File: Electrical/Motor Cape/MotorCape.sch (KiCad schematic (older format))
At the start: 15 parts, among them J1 back_right motor, J11 flag_wheel servo, J2 front_right motor, J3 back_left motor, J4 front_left motor, J5 draw_bridge motor, J6 flag_wheel motor, J7 i2c bus connector, J9 Raspberry_Pi_2_3, U1 MotorControl Left, U2 MotorControl Right, U3 MotorControl Top

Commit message: worked more on motor cape
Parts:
- removed U1: MotorControl Left, symbol MotorControl
- removed U2: MotorControl Right, symbol MotorControl
- removed U3: MotorControl Top, symbol MotorControl
- added P1: Shifter_Front_HI, Pin_Headers:Pin_Header_Straight_1x06, symbol CONN_01X06
- added P10: Controller 2_2, Terminal_Blocks:TerminalBlock_Pheonix_MPT-2.54mm_6pol, symbol CONN_01X06
- added P11: Controller 3_1, Pin_Headers:Pin_Header_Straight_1x05, symbol CONN_01X05
- added P12: Controller 3_2, Terminal_Blocks:TerminalBlock_Pheonix_MPT-2.54mm_6pol, symbol CONN_01X06
- added P2: Shifter_Front_LO, Pin_Headers:Pin_Header_Straight_1x06, symbol CONN_01X06
- added P3: Shifter_Back_HI, Pin_Headers:Pin_Header_Straight_1x06, symbol CONN_01X06
- added P4: Shifter_Back_LO, Pin_Headers:Pin_Header_Straight_1x06, symbol CONN_01X06
- added P5: Shifter_Misc_HI, Pin_Headers:Pin_Header_Straight_1x06, symbol CONN_01X06
- added P6: Shifter_Misc_LO, Pin_Headers:Pin_Header_Straight_1x06, symbol CONN_01X06
- added P7: Controller 1_1, Pin_Headers:Pin_Header_Straight_1x05, symbol CONN_01X05
- added P8: Controller 1_2, Terminal_Blocks:TerminalBlock_Pheonix_MPT-2.54mm_6pol, symbol CONN_01X06
- added P9: Controller 2_1, Pin_Headers:Pin_Header_Straight_1x05, symbol CONN_01X05
- ARD1: footprint (none) -> MotorCapeComponents:Arduino_Due_Shield
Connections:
- net labels removed: BL_A-H, BL_A-L, BL_B-H, BL_B-L, BR_A-H, BR_A-L, BR_B-H, BR_B-L, DB_A-H, DB_A-L, DB_B-H, DB_B-L, FL_A-L, FL_B-L, FR_A-H, FR_A-L, FR_B-H, FR_B-L, FW_A-H, FW_A-L, FW_B-H, FW_B-L
- wire segments 110 -> 247
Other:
- moved on the sheet: J2

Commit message: added gud stuff
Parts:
- removed Battery1: pcie_8pin power connector, symbol Conn_02x04_Top_Bottom
- added P13: battery stuff, Pin_Headers:Pin_Header_Straight_1x02, symbol CONN_01X02
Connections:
- net +5V: no longer P2.4 (P4), P4.4 (P4), P6.4 (P4)
- net Earth: now also P13.2 (P2)
- net +12V: now reaches F1.2
- net +12V: now also P13.1 (P1)
- new net +3V3: P2.4 (P4), P4.4 (P4), P6.4 (P4)
- no-connect marks 88 -> 89
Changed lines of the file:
@@
-$EndComp
-$Comp
-L Conn_02x04_Top_Bottom Battery1
-U 1 1 5A6B59ED
-P 1500 2950
-F 0 "Battery1" H 1550 3150 50  0000 C CNN
-F 1 "pcie_8pin power connector" H 1550 2650 50  0000 C CNN
-F 2 "" H 1500 2950 50  0001 C CNN
-F 3 "" H 1500 2950 50  0001 C CNN
-	1    1500 2950
-	-1   0    0    1
 $EndComp
 $Comp
@@
 F1 "level_shifters.sch" 60
 $EndSheet
-Text GLabel 3150 3500 2    60   Input ~ 0
-FL_B-H
-Text GLabel 3150 3600 2    60   Input ~ 0
-FL_A-H
 $Comp
 L Raspberry_Pi_2_3 J9
@@
 Text GLabel 2200 2900 2    60   Input ~ 0
 MOTOR_PWR
-Text GLabel 2200 3100 2    60   Input ~ 0
+Text GLabel 1250 2700 0    60   Input ~ 0
 MOTOR_GND
-$Comp
-L Arduino_Due_Shield ARD1
-U 1 1 5A86C034
-P 5850 2400
-F 0 "ARD1" V 5950 2400 60  0000 C CNN
-F 1 "Arduino_Due_Shield" V 5750 2400 60  0000 C CNN
-F 2 "MotorCapeComponents:Arduino_Due_Shield" H 6550 5150 60  0001 C CNN
-F 3 "" H 6550 5150 60  0001 C CNN
-	1    5850 2400
-	0    1    1    0
-$EndComp
 $Comp
 L CONN_01X06 P1
@@
 $EndComp
 $Comp
-L +5V #PWR026
-U 1 1 5A8FD9AD
-P 9300 4350
-F 0 "#PWR026" H 9300 4200 50  0001 C CNN
-F 1 "+5V" H 9300 4490 50  0000 C CNN
-F 2 "" H 9300 4350 50  0001 C CNN
-F 3 "" H 9300 4350 50  0001 C CNN
-	1    9300 4350
-	1    0    0    -1
-$EndComp
-$Comp
-L Earth #PWR027
+L Earth #PWR026
 U 1 1 5A8FD9EB
 P 9400 4350
-F 0 "#PWR027" H 9400 4100 50  0001 C CNN
+F 0 "#PWR026" H 9400 4100 50  0001 C CNN
 F 1 "Earth" H 9400 4200 50  0001 C CNN
 F 2 "" H 9400 4350 50  0001 C CNN
@@
 $EndComp
 $Comp
-L Earth #PWR028
+L Earth #PWR027
 U 1 1 5A901DF0
 P 6600 7200
-F 0 "#PWR028" H 6600 6950 50  0001 C CNN
+F 0 "#PWR027" H 6600 6950 50  0001 C CNN
 F 1 "Earth" H 6600 7050 50  0001 C CNN
 F 2 "" H 6600 7200 50  0001 C CNN
@@
 $EndComp
 $Comp
-L Earth #PWR029
+L Earth #PWR028
 U 1 1 5A901E80
 P 6600 6800
-F 0 "#PWR029" H 6600 6550 50  0001 C CNN
+F 0 "#PWR028" H 6600 6550 50  0001 C CNN
 F 1 "Earth" H 6600 6650 50  0001 C CNN
 F 2 "" H 6600 6800 50  0001 C CNN
@@
 $EndComp
 $Comp
-L +5V #PWR030
-U 1 1 5A901F49
-P 6500 7200
-F 0 "#PWR030" H 6500 7050 50  0001 C CNN
-F 1 "+5V" H 6500 7340 50  0000 C CNN
-F 2 "" H 6500 7200 50  0001 C CNN
-F 3 "" H 6500 7200 50  0001 C CNN
-	1    6500 7200
-	1    0    0    -1
-$EndComp
-$Comp
-L +5V #PWR031
+L +5V #PWR029
 U 1 1 5A902038
 P 6500 6800
-F 0 "#PWR031" H 6500 6650 50  0001 C CNN
+F 0 "#PWR029" H 6500 6650 50  0001 C CNN
 F 1 "+5V" H 6500 6940 50  0000 C CNN
 F 2 "" H 6500 6800 50  0001 C CNN
@@
 $EndComp
 $Comp
-L +5V #PWR032
+L +5V #PWR030
 U 1 1 5A906051
 P 1100 5250
-F 0 "#PWR032" H 1100 5100 50  0001 C CNN
+F 0 "#PWR030" H 1100 5100 50  0001 C CNN
 F 1 "+5V" H 1100 5390 50  0000 C CNN
 F 2 "" H 1100 5250 50  0001 C CNN
@@
 $EndComp
 $Comp
-L +5V #PWR033
-U 1 1 5A90614E
-P 1100 5950
-F 0 "#PWR033" H 1100 5800 50  0001 C CNN
-F 1 "+5V" H 1100 6090 50  0000 C CNN
-F 2 "" H 1100 5950 50  0001 C CNN
-F 3 "" H 1100 5950 50  0001 C CNN
-	1    1100 5950
-	-1   0    0    -1
-$EndComp
-$Comp
-L Earth #PWR034
+L Earth #PWR031
 U 1 1 5A9062E9
 P 1200 5250
-F 0 "#PWR034" H 1200 5000 50  0001 C CNN
+F 0 "#PWR031" H 1200 5000 50  0001 C CNN
 F 1 "Earth" H 1200 5100 50  0001 C CNN
 F 2 "" H 1200 5250 50  0001 C CNN
@@
 $EndComp
 $Comp
-L Earth #PWR035
+L Earth #PWR032
 U 1 1 5A906333
 P 1200 5950
-F 0 "#PWR035" H 1200 5700 50  0001 C CNN
+F 0 "#PWR032" H 1200 5700 50  0001 C CNN
 F 1 "Earth" H 1200 5800 50  0001 C CNN
 F 2 "" H 1200 5950 50  0001 C CNN
@@
 Wire Wire Line
 	3650 6200 3650 6450
+$Comp
+L +3.3V #PWR033
+U 1 1 5A98D0A1
+P 10350 4400
+F 0 "#PWR033" H 10350 4250 50  0001 C CNN
+F 1 "+3.3V" H 10350 4540 50  0000 C CNN
+F 2 "" H 10350 4400 50  0000 C CNN
+F 3 "" H 10350 4400 50  0000 C CNN
+	1    10350 4400
+	-1   0    0    1
+$EndComp
+$Comp
+L +3.3V #PWR034
+U 1 1 5A98D26D
+P 6500 7200
+F 0 "#PWR034" H 6500 7050 50  0001 C CNN
+F 1 "+3.3V" H 6500 7340 50  0000 C CNN
+F 2 "" H 6500 7200 50  0000 C CNN
+F 3 "" H 6500 7200 50  0000 C CNN
+	1    6500 7200
+	1    0    0    -1
+$EndComp
+$Comp
+L +3.3V #PWR035
+U 1 1 5A98D68F
+P 1100 5950
+F 0 "#PWR035" H 1100 5800 50  0001 C CNN
+F 1 "+3.3V" H 1100 6090 50  0000 C CNN
+F 2 "" H 1100 5950 50  0000 C CNN
+F 3 "" H 1100 5950 50  0000 C CNN
+	1    1100 5950
+	1    0    0    -1
+$EndComp
+$Comp
+L CONN_01X02 P13
+U 1 1 5A98ECA7
+P 1550 2850
+F 0 "P13" H 1550 3000 50  0000 C CNN
+F 1 "battery stuff" V 1650 2850 50  0000 C CNN
+F 2 "Pin_Headers:Pin_Header_Straight_1x02" H 1550 2850 50  0001 C CNN
+F 3 "" H 1550 2850 50  0000 C CNN
+	1    1550 2850
+	-1   0    0    1
+$EndComp
+$Comp
+L +12V #PWR036
+U 1 1 5A98F2CD
+P 1750 2900
+F 0 "#PWR036" H 1750 2750 50  0001 C CNN
+F 1 "+12V" H 1750 3040 50  0000 C CNN
+F 2 "" H 1750 2900 50  0000 C CNN
+F 3 "" H 1750 2900 50  0000 C CNN
+	1    1750 2900
+	-1   0    0    1
+$EndComp
+$Comp
+L Earth #PWR037
+U 1 1 5A98F376
+P 1750 2750
+F 0 "#PWR037" H 1750 2500 50  0001 C CNN
+F 1 "Earth" H 1750 2600 50  0001 C CNN
+F 2 "" H 1750 2750 50  0001 C CNN
+F 3 "" H 1750 2750 50  0001 C CNN
+	1    1750 2750
+	1    0    0    1
+$EndComp
+Wire Wire Line
+	1900 2900 1750 2900
+Wire Wire Line
+	1750 2800 1750 2750
+NoConn ~ 5000 1200
+$Comp
+L PWR_FLAG #FLG038
+U 1 1 5A9910A8
+P 1850 3250
+F 0 "#FLG038" H 1850 3345 50  0001 C CNN
+F 1 "PWR_FLAG" H 1850 3430 50  0000 C CNN
+F 2 "" H 1850 3250 50  0000 C CNN
+F 3 "" H 1850 3250 50  0000 C CNN
+	1    1850 3250
+	-1   0    0    1
+$EndComp
+Wire Wire Line
+	1850 3250 1850 2900
+Connection ~ 1850 2900
+$Comp
+L PWR_FLAG #FLG039
+U 1 1 5A991593
+P 10050 4350
+F 0 "#FLG039" H 10050 4445 50  0001 C CNN
+F 1 "PWR_FLAG" H 10050 4530 50  0000 C CNN
+F 2 "" H 10050 4350 50  0000 C CNN
+F 3 "" H 10050 4350 50  0000 C CNN
+	1    10050 4350
+	-1   0    0    1
+$EndComp
+Wire Wire Line
+	10350 4400 10350 4350
+Wire Wire Line
+	10350 4350 10050 4350
+Wire Wire Line
+	10050 4350 10050 4200
+Wire Wire Line
+	10050 4200 9300 4200
+Wire Wire Line
+	9300 4200 9300 4350
+$Comp
+L Arduino_Due_Shield ARD1
+U 1 1 5A993409
+P 5850 2400
+F 0 "ARD1" V 5950 2400 60  0000 C CNN
+F 1 "Arduino_Due_Shield" V 5750 2400 60  0000 C CNN
+F 2 "MotorCapeComponents:Arduino_Due_Shield" H 6550 5150 60  0001 C CNN
+F 3 "" H 6550 5150 60  0001 C CNN
+	1    5850 2400
+	0    1    1    0
+$EndComp
 $EndSCHEMATC

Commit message: pushing aldriges changes to arduino board
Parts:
- removed J9: Raspberry_Pi_2_3, Pin_Headers:Pin_Header_Straight_2x20, symbol Raspberry_Pi_2_3
- added P14: CONN_01X04, Pin_Headers:Pin_Header_Straight_1x04, symbol CONN_01X04
- added U1: IMU, MotorCapeComponents:IMU, symbol IMU
- F1: footprint (none) -> Fuse_Holders_and_Fuses:Fuseholder5x20_horiz_open_inline_Type-I
- J7: footprint (none) -> Pin_Headers:Pin_Header_Straight_1x02
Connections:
- net +3V3: now also U1.11 (3.3V)
- net +5V: now also ARD1.5 (5V), P14.1 (P1); no longer ARD1.92 (SPI_5V)
- net Earth: now also ARD1.6 (GND), P14.2 (P2), U1.10 (GND); no longer ARD1.90 (SPI_GND)
- net FROM_Pi: now also P14.4 (P4)
- net SCL: now also U1.13 (SCL)
- net SDA: now also U1.12 (SDA)
- net TO_Pi: now also P14.3 (P3)
- no-connect marks 89 -> 70
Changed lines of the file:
@@
 F 0 "J7" H 8950 700 50  0000 C CNN
 F 1 "i2c bus connector" H 9000 1050 50  0000 C CNN
-F 2 "" H 8950 900 50  0001 C CNN
+F 2 "Pin_Headers:Pin_Header_Straight_1x02" H 8950 900 50  0001 C CNN
 F 3 "" H 8950 900 50  0001 C CNN
 	1    8950 900
@@
 NoConn ~ 3700 1100
 NoConn ~ 3800 1100
+NoConn ~ 4100 1100
 NoConn ~ 3900 1100
-NoConn ~ 4000 1100
-NoConn ~ 4100 1100
 NoConn ~ 4200 1100
 NoConn ~ 4300 1100
 NoConn ~ 4400 1100
 NoConn ~ 4500 1100
-NoConn ~ 4600 1100
 NoConn ~ 4800 1100
 NoConn ~ 4900 1100
@@
 F1 "level_shifters.sch" 60
 $EndSheet
-$Comp
-L Raspberry_Pi_2_3 J9
-U 1 1 5A6BC98A
-P 10250 2300
-F 0 "J9" H 10950 1050 50  0000 C CNN
-F 1 "Raspberry_Pi_2_3" H 9850 3200 50  0000 C CNN
-F 2 "Pin_Headers:Pin_Header_Straight_2x20" H 11250 3550 50  0001 C CNN
-F 3 "" H 10300 2150 50  0001 C CNN
-	1    10250 2300
-	-1   0    0    -1
-$EndComp
-Text GLabel 9350 3100 0    60   Input ~ 0
-TO_Pi
-Text GLabel 9350 3000 0    60   Input ~ 0
-FROM_Pi
 Text GLabel 7900 1100 1    60   Input ~ 0
 TO_Pi
@@
 L +5V #PWR022
 U 1 1 5A6BDFCD
-P 8450 2450
-F 0 "#PWR022" H 8450 2300 50  0001 C CNN
-F 1 "+5V" H 8450 2590 50  0000 C CNN
-F 2 "" H 8450 2450 50  0001 C CNN
-F 3 "" H 8450 2450 50  0001 C CNN
-	1    8450 2450
-	0    1    1    0
+P 4000 1100
+F 0 "#PWR022" H 4000 950 50  0001 C CNN
+F 1 "+5V" H 4000 1240 50  0000 C CNN
+F 2 "" H 4000 1100 50  0001 C CNN
+F 3 "" H 4000 1100 50  0001 C CNN
+	1    4000 1100
+	1    0    0    -1
 $EndComp
 $Comp
 L Earth #PWR023
 U 1 1 5A6BE144
-P 8450 2550
-F 0 "#PWR023" H 8450 2300 50  0001 C CNN
-F 1 "Earth" H 8450 2400 50  0001 C CNN
-F 2 "" H 8450 2550 50  0001 C CNN
-F 3 "" H 8450 2550 50  0001 C CNN
-	1    8450 2550
-	0    -1   -1   0
+P 4600 1100
+F 0 "#PWR023" H 4600 850 50  0001 C CNN
+F 1 "Earth" H 4600 950 50  0001 C CNN
+F 2 "" H 4600 1100 50  0001 C CNN
+F 3 "" H 4600 1100 50  0001 C CNN
+	1    4600 1100
+	-1   0    0    1
 $EndComp
 Text GLabel 8750 900  0    60   Input ~ 0
@@
 Text GLabel 7000 1100 1    60   Input ~ 0
 SDA
-Text GLabel 9350 1500 0    60   Input ~ 0
-SCL
-Text GLabel 9350 1400 0    60   Input ~ 0
-SDA
-NoConn ~ 11150 1600
-NoConn ~ 11150 1700
-NoConn ~ 11150 1800
-NoConn ~ 11150 1900
-NoConn ~ 11150 2000
-NoConn ~ 11150 2100
-NoConn ~ 11150 2200
-NoConn ~ 11150 2300
-NoConn ~ 11150 2400
-NoConn ~ 11150 2500
-NoConn ~ 11150 2600
-NoConn ~ 11150 2700
-NoConn ~ 11150 3000
-NoConn ~ 11150 3100
-NoConn ~ 10650 3600
-NoConn ~ 10550 3600
-NoConn ~ 10450 3600
-NoConn ~ 10350 3600
-NoConn ~ 10250 3600
-NoConn ~ 10150 3600
-NoConn ~ 10050 3600
-NoConn ~ 9950 3600
-NoConn ~ 10050 1000
-NoConn ~ 10150 1000
-NoConn ~ 10350 1000
-NoConn ~ 10450 1000
-NoConn ~ 9350 1600
-NoConn ~ 9350 1800
-NoConn ~ 9350 1900
-NoConn ~ 9350 2100
-NoConn ~ 9350 2700
-NoConn ~ 9350 2800
+NoConn ~ 8450 2450
+NoConn ~ 8450 2550
 Text GLabel 3400 6500 0    60   Input ~ 0
 MOTOR_PWR
@@
 F 0 "F1" V 2130 2900 50  0000 C CNN
 F 1 "Fuse" V 1975 2900 50  0000 C CNN
-F 2 "" V 1980 2900 50  0001 C CNN
+F 2 "Fuse_Holders_and_Fuses:Fuseholder5x20_horiz_open_inline_Type-I" V 1980 2900 50  0001 C CNN
 F 3 "" H 2050 2900 50  0001 C CNN
 	1    2050 2900
@@
 	6700 4950 9850 4950
 Wire Wire Line
-	8450 2650 9150 2650
-Wire Wire Line
-	8450 2350 9200 2350
-Wire Wire Line
-	9200 2350 9200 2500
-Wire Wire Line
-	9200 2500 9350 2500
-Wire Wire Line
-	9350 2400 9250 2400
-Wire Wire Line
-	9250 2400 9250 2250
-Wire Wire Line
-	9250 2250 8450 2250
-Wire Wire Line
-	8450 2150 9300 2150
-Wire Wire Line
-	9300 2150 9300 2300
-Wire Wire Line
-	9300 2300 9350 2300
-Wire Wire Line
-	9150 2650 9150 2200
-Wire Wire Line
-	9150 2200 9350 2200
-Wire Wire Line
 	9600 3950 10650 3950
 Wire Wire Line
@@
 	0    1    1    0
 $EndComp
+$Comp
+L CONN_01X04 P14
+U 1 1 5AA1DD33
+P 10400 1650
+F 0 "P14" H 10400 1900 50  0000 C CNN
+F 1 "CONN_01X04" V 10500 1650 50  0000 C CNN
+F 2 "Pin_Headers:Pin_Header_Straight_1x04" H 10400 1650 50  0001 C CNN
+F 3 "" H 10400 1650 50  0000 C CNN
+	1    10400 1650
+	1    0    0    -1
+$EndComp
+Text GLabel 10200 1700 0    60   Input ~ 0
+TO_Pi
+Text GLabel 10200 1800 0    60   Input ~ 0
+FROM_Pi
+$Comp
+L +5V #PWR040
+U 1 1 5AA1DEF8
+P 10200 1500
+F 0 "#PWR040" H 10200 1350 50  0001 C CNN
+F 1 "+5V" H 10200 1640 50  0000 C CNN
+F 2 "" H 10200 1500 50  0001 C CNN
+F 3 "" H 10200 1500 50  0001 C CNN
+	1    10200 1500
+	0    -1   -1   0
+$EndComp
+$Comp
+L Earth #PWR041
+U 1 1 5AA1DF4B
+P 10200 1600
+F 0 "#PWR041" H 10200 1350 50  0001 C CNN
+F 1 "Earth" H 10200 1450 50  0001 C CNN
+F 2 "" H 10200 1600 50  0001 C CNN
+F 3 "" H 10200 1600 50  0001 C CNN
+	1    10200 1600
+	0    1    1    0
+$EndComp
+NoConn ~ 8450 2150
+NoConn ~ 8450 2250
+NoConn ~ 8450 2350
+NoConn ~ 8450 2650
+$Comp
+L IMU U1
+U 1 1 5AA1F45A
+P 9250 2200
+F 0 "U1" H 9650 2250 60  0000 C CNN
+F 1 "IMU" H 9650 2350 60  0000 C CNN
+F 2 "MotorCapeComponents:IMU" H 9250 2200 60  0001 C CNN
+F 3 "" H 9250 2200 60  0000 C CNN
+	1    9250 2200
+	1    0    0    -1
+$EndComp
+$Comp
+L Earth #PWR042
+U 1 1 5AA1F5F0
+P 10350 2550
+F 0 "#PWR042" H 10350 2300 50  0001 C CNN
+F 1 "Earth" H 10350 2400 50  0001 C CNN
+F 2 "" H 10350 2550 50  0001 C CNN
+F 3 "" H 10350 2550 50  0001 C CNN
+	1    10350 2550
+	0    -1   -1   0
+$EndComp
+$Comp
+L +3.3V #PWR043
+U 1 1 5AA1F998
+P 10350 2650
+F 0 "#PWR043" H 10350 2500 50  0001 C CNN
+F 1 "+3.3V" H 10350 2790 50  0000 C CNN
+F 2 "" H 10350 2650 50  0000 C CNN
+F 3 "" H 10350 2650 50  0000 C CNN
+	1    10350 2650
+	0    1    1    0
+$EndComp
+NoConn ~ 9050 2250
+NoConn ~ 9050 2350
+NoConn ~ 9050 2450
+NoConn ~ 9050 2550
+NoConn ~ 9050 2650
+NoConn ~ 9050 2750
+NoConn ~ 9050 2950
+NoConn ~ 9050 2850
+NoConn ~ 9050 3050
+Text GLabel 10350 2750 2    60   Input ~ 0
+SDA
+Text GLabel 10350 2850 2    60   Input ~ 0
+SCL
 $EndSCHEMATC

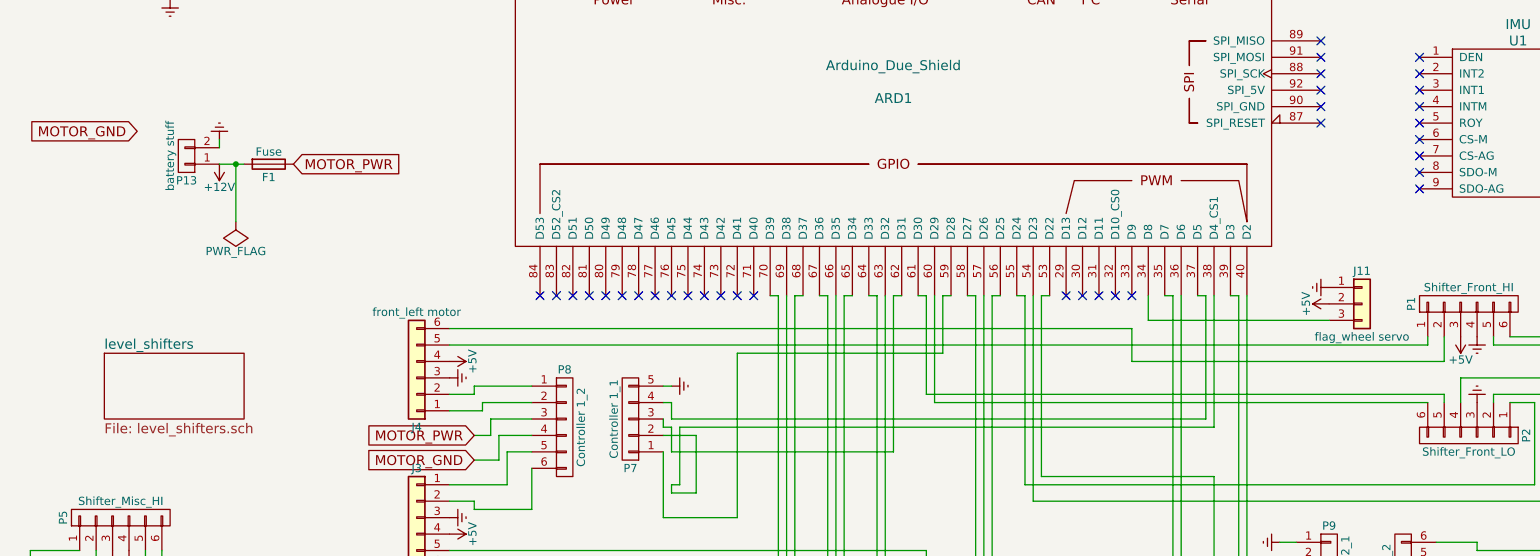
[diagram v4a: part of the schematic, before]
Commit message: finished updates on pi schematic, working on footprints next
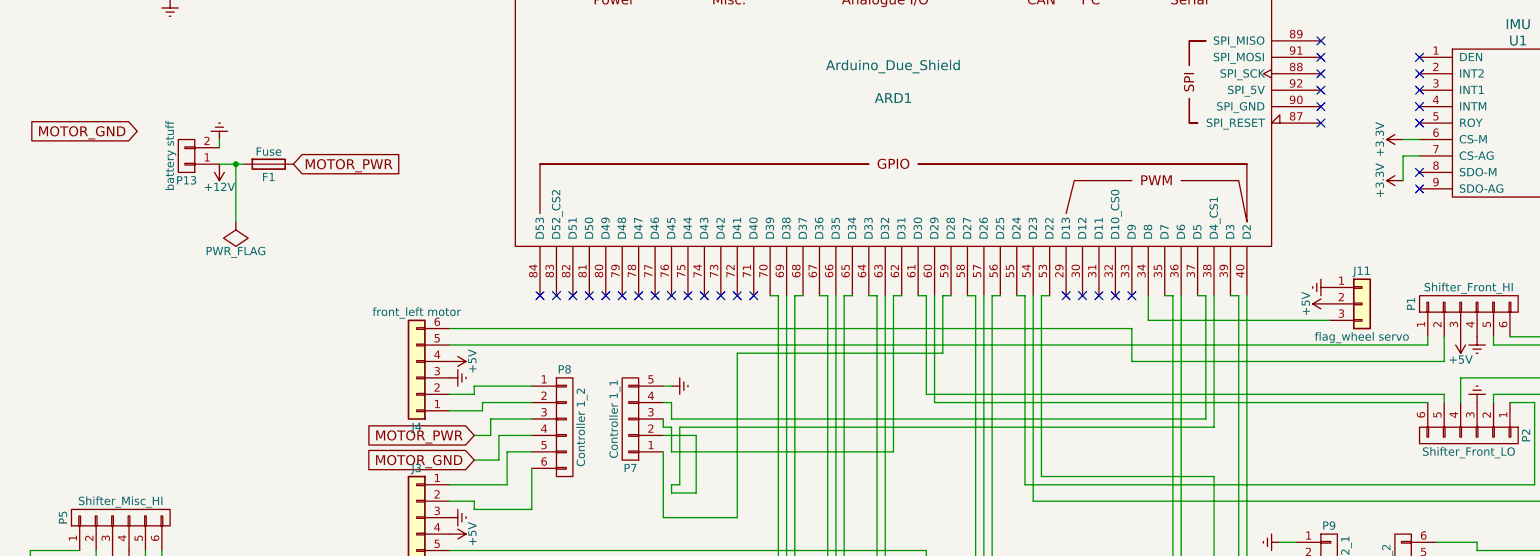
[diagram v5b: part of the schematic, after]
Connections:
- net +3V3: now also U1.6 (CS-M), U1.7 (CS-AG)
- no-connect marks 70 -> 68
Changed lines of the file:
@@
 NoConn ~ 7400 1100
 NoConn ~ 7300 1100
-$Sheet
-S 1050 4050 850  400
-U 5A6D7E85
-F0 "level_shifters" 60
-F1 "level_shifters.sch" 60
-$EndSheet
 Text GLabel 7900 1100 1    60   Input ~ 0
 TO_Pi
@@
 $EndComp
 Wire Wire Line
-	1900 2900 1750 2900
+	1750 2900 1900 2900
 Wire Wire Line
 	1750 2800 1750 2750
@@
 NoConn ~ 9050 2550
 NoConn ~ 9050 2650
-NoConn ~ 9050 2750
 NoConn ~ 9050 2950
-NoConn ~ 9050 2850
 NoConn ~ 9050 3050
 Text GLabel 10350 2750 2    60   Input ~ 0
@@
 Text GLabel 10350 2850 2    60   Input ~ 0
 SCL
+$Comp
+L +3.3V #PWR?
+U 1 1 5AAB580D
+P 8950 3000
+F 0 "#PWR?" H 8950 2850 50  0001 C CNN
+F 1 "+3.3V" H 8950 3140 50  0000 C CNN
+F 2 "" H 8950 3000 50  0000 C CNN
+F 3 "" H 8950 3000 50  0000 C CNN
+	1    8950 3000
+	0    -1   -1   0
+$EndComp
+$Comp
+L +3.3V #PWR?
+U 1 1 5AAB58EE
+P 8950 2750
+F 0 "#PWR?" H 8950 2600 50  0001 C CNN
+F 1 "+3.3V" H 8950 2890 50  0000 C CNN
+F 2 "" H 8950 2750 50  0000 C CNN
+F 3 "" H 8950 2750 50  0000 C CNN
+	1    8950 2750
+	0    -1   -1   0
+$EndComp
+Wire Wire Line
+	8950 3000 8950 2850
+Wire Wire Line
+	8950 2850 9050 2850
+Wire Wire Line
+	9050 2750 8950 2750
 $EndSCHEMATC
